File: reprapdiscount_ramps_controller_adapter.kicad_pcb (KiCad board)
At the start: 2 copper layers, 62.1 x 21.2 mm, 7 parts

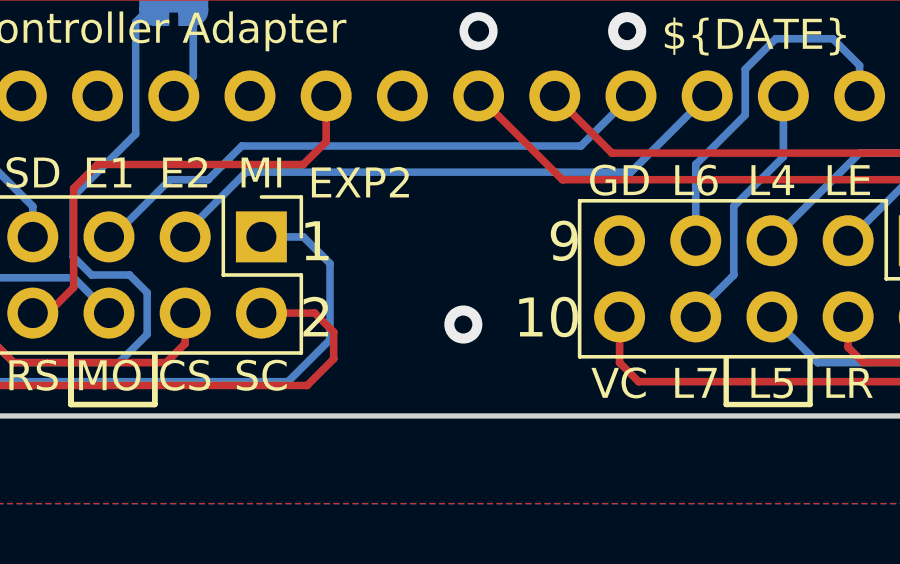
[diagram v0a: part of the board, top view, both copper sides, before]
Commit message: all: add oshw logo to design
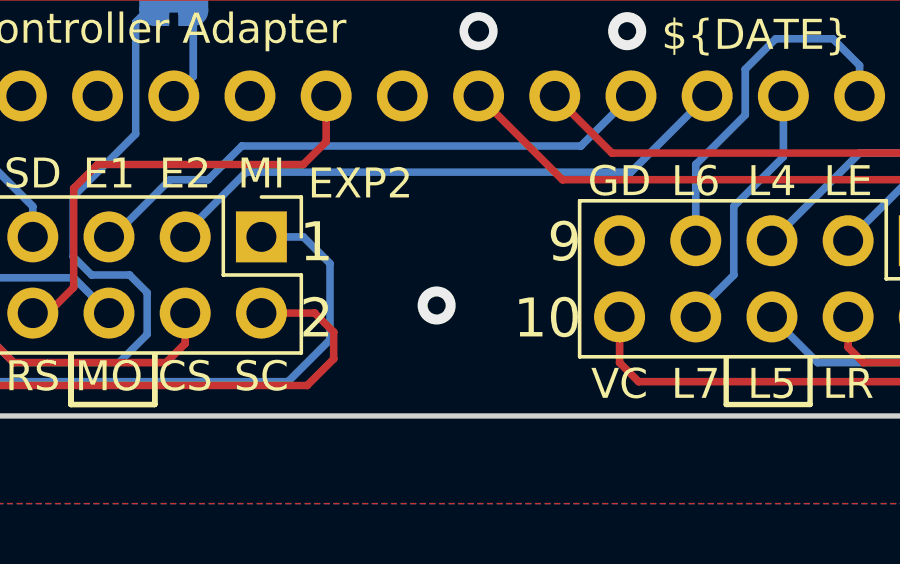
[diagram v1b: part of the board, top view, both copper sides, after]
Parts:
- added SYM1: Logo_Open_Hardware_Large, Gigahawk:OSHW-Logo2_7.3x6mm_Mask, F.Cu at (103.6, -55.7)
